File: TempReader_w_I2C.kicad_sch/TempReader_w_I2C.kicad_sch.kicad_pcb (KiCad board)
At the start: 4 copper layers, 40 x 47 mm, 42 parts, among them J1 NRF Pin Header, J2 BME Pin Header, U5 MIC5205-3.3YM5, Y1 16MH

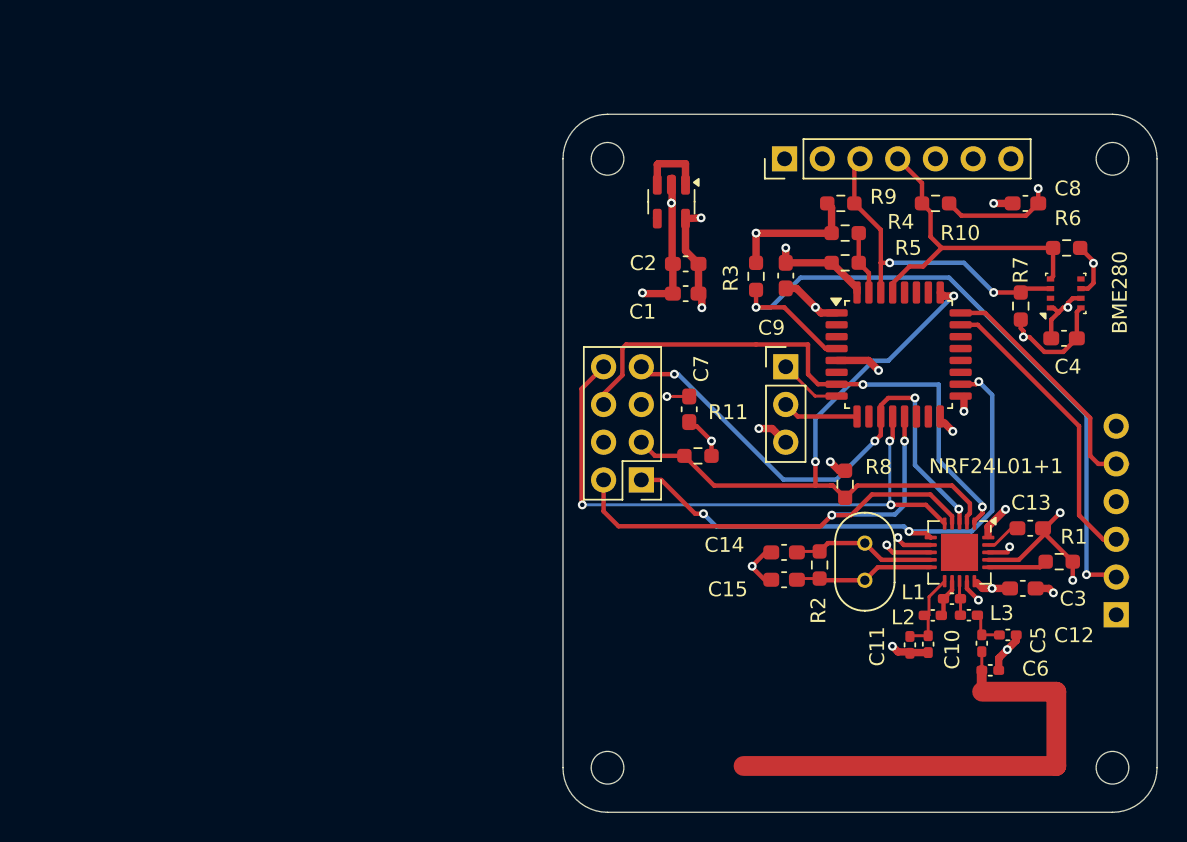
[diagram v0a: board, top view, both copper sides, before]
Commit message: Added debug prints for UART
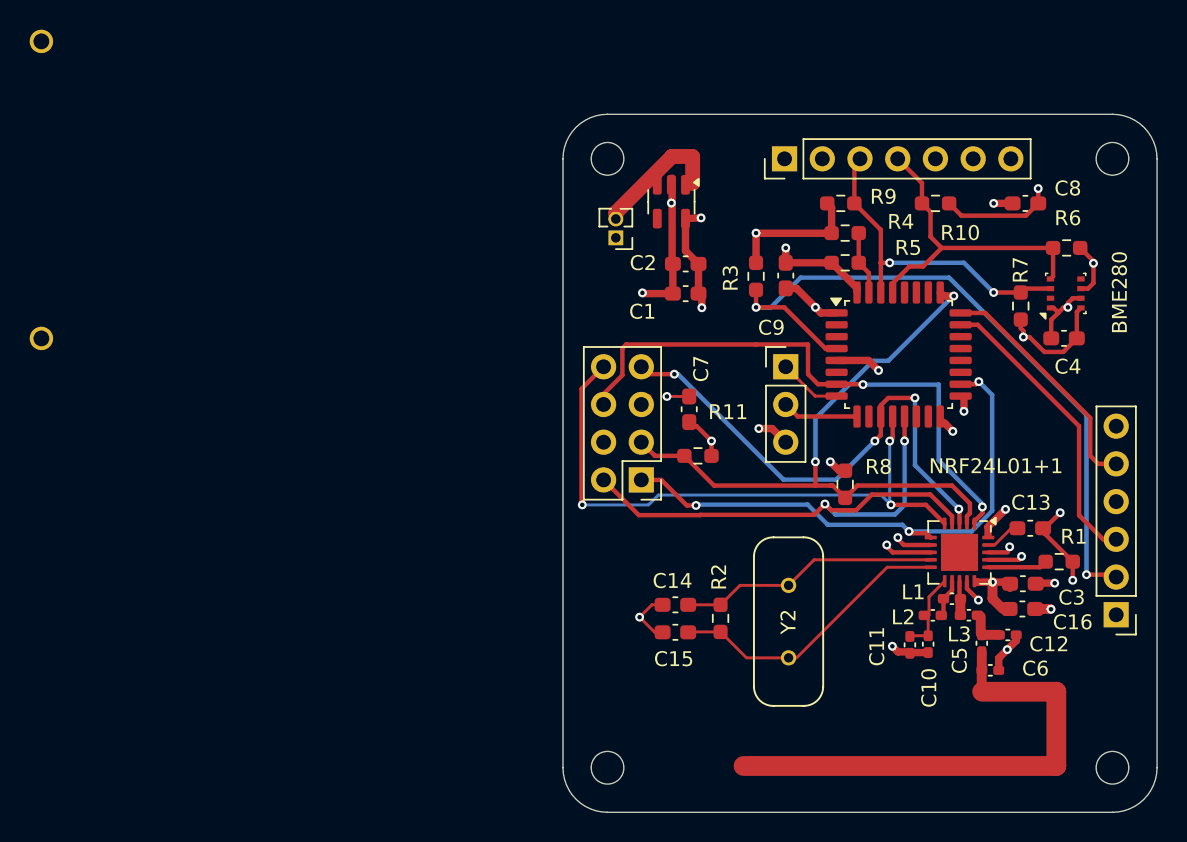
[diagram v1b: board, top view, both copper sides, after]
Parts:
- removed Y1: 16MH, ECS-160-20-46X:XTAL_ECS-160-20-46X
- added B1: BS-3, KiCADv6:BS-3_MPD, B.Cu at (119.9, 78.6)
- added C16: 10uF, Capacitor_SMD:C_0603_1608Metric_Pad1.08x0.95mm_HandSolder, F.Cu at (185.9, 103.3)
- added J3: PowerHeader, Connector_PinHeader_1.27mm:PinHeader_1x02_P1.27mm_Vertical, F.Cu at (158.6, 78.3)
- added Y2: 16Mhz, ECS-160-12-4X-GM:XTAL_ECS-160-12-4X-GM, F.Cu at (170.2, 104.2)
- STLinkHeader1: renamed from NotSure1; moved to F.Cu
- moved C15 8.13 mm to (162.6, 104.9)
- moved C14 8.13 mm to (162.6, 103.0)
- moved R2 7.58 mm to (165.6, 103.9)
- moved C3 0.32 mm to (186.0, 101.6)
- turned STLinkHeader1 to 180 degrees
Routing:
- net Net-(NRF24L01+1-XC1): track 9.46 -> 19.1 mm
- net Net-(NRF24L01+1-XC2): track 9.74 -> 17.6 mm
- net PowerIn: track 4.70 -> 9.25 mm
- net +3V3: track 57.3 -> 58.6 mm
- net GND1: track 56.4 -> 55.4 mm, vias 17 -> 19
- net SPI_MOSI: track 39.1 -> 38.3 mm
- net SW_DIO: track 20.7 -> 20.0 mm
- net SW_CLK: track 16.9 -> 16.2 mm
- net NRST: track 48.2 -> 47.5 mm
- net SPI_MISO: track 41.0 -> 41.6 mm

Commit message: Slightly change comments
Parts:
- removed B1: BS-3, KiCADv6:BS-3_MPD
- removed H2: MountingHole, MountingHole:MountingHole_2.2mm_M2
- added C17: 100 nF, Capacitor_SMD:C_0603_1608Metric_Pad1.08x0.95mm_HandSolder, F.Cu at (157.4, 92.9)
- added SW1: D6R90F2LFS, footprints:D6R90_CNK, F.Cu at (158.9, 83.0)
- J1: footprint Connector_PinHeader_2.54mm:PinHeader_2x04_P2.54mm_Vertical -> footprints:CON8_2X4_TU_SSQ
- J3: footprint Connector_PinHeader_1.27mm:PinHeader_1x02_P1.27mm_Vertical -> Connector_PinHeader_2.54mm:PinHeader_1x02_P2.54mm_Vertical
- R5: value 0 -> 10k
- moved C15 11.0 mm to (173.6, 104.7), turned to -90 degrees
- moved C1 7.72 mm to (165.5, 74.7), turned to 90 degrees
- moved J1 6.97 mm to (159.1, 101.5), turned to -90 degrees
- moved C2 6.82 mm to (167.4, 74.6), turned to 90 degrees
- moved C14 5.82 mm to (168.1, 104.9), turned to -90 degrees
- moved R2 5.16 mm to (170.8, 103.8), turned to 0 degrees
- moved C7 3.88 mm to (162.9, 93.7)
- moved Y2 3.80 mm to (171.1, 100.5), turned to 0 degrees
- moved J3 2.72 mm to (157.9, 75.7)
- moved R11 2.36 mm to (166.3, 93.7), turned to 0 degrees
- moved R3 0.33 mm to (168.3, 80.9)
- moved U5 0.10 mm to (162.4, 75.9)
- turned C8 to 0 degrees
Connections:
- BME280 pad 2: unconnected-(BME280-CSB-Pad2) -> BME_CSB
- BME280 pad 5: unconnected-(BME280-SDO-Pad5) -> BME_SDO
- J1 pad 1: NRF_IRQ -> +3V3
- J1 pad 2: SPI_MOSI -> GND1
- J1 pad 4: +3V3 -> NRF_CE
- J1 pad 5: GND1 -> SPI_MOSI
- J1 pad 6: NRF_CE -> SPI_SCK
- J1 pad 7: SPI_SCK -> NRF_IRQ
- J2 pad 1: unconnected-(J2-Pin_1-Pad1) -> BME_CSB
- J2 pad 2: unconnected-(J2-Pin_2-Pad2) -> I2C_SDA
- J2 pad 3: I2C_SDA -> BME_SDO
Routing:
- net BME_CSB: track 0.00 -> 21.9 mm, vias 0 -> 1
- net BME_SDO: track 0.00 -> 19.1 mm, vias 0 -> 1
- net NRST: track 47.5 -> 64.9 mm
- net NRF_CE: track 38.8 -> 54.5 mm
- net SPI_MISO: track 41.6 -> 28.0 mm, vias 3 -> 2
- net NRF_IRQ: track 37.7 -> 49.8 mm, vias 3 -> 2
- net +3V3: track 58.6 -> 52.1 mm
- net CS_NRF: track 44.2 -> 50.7 mm
- net Net-(NRF24L01+1-XC1): track 19.1 -> 14.6 mm
- net SPI_SCK: track 36.1 -> 33.8 mm
- net GND1: track 55.4 -> 53.4 mm, vias 19 -> 23
- net SPI_MOSI: track 38.3 -> 39.6 mm
- net I2C_SDA: track 22.3 -> 23.0 mm
- added copper zone on B.Cu, net GND1
- added copper zone on F.Cu, net GND1
